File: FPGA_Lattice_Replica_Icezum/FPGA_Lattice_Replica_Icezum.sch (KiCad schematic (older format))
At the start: 0 parts

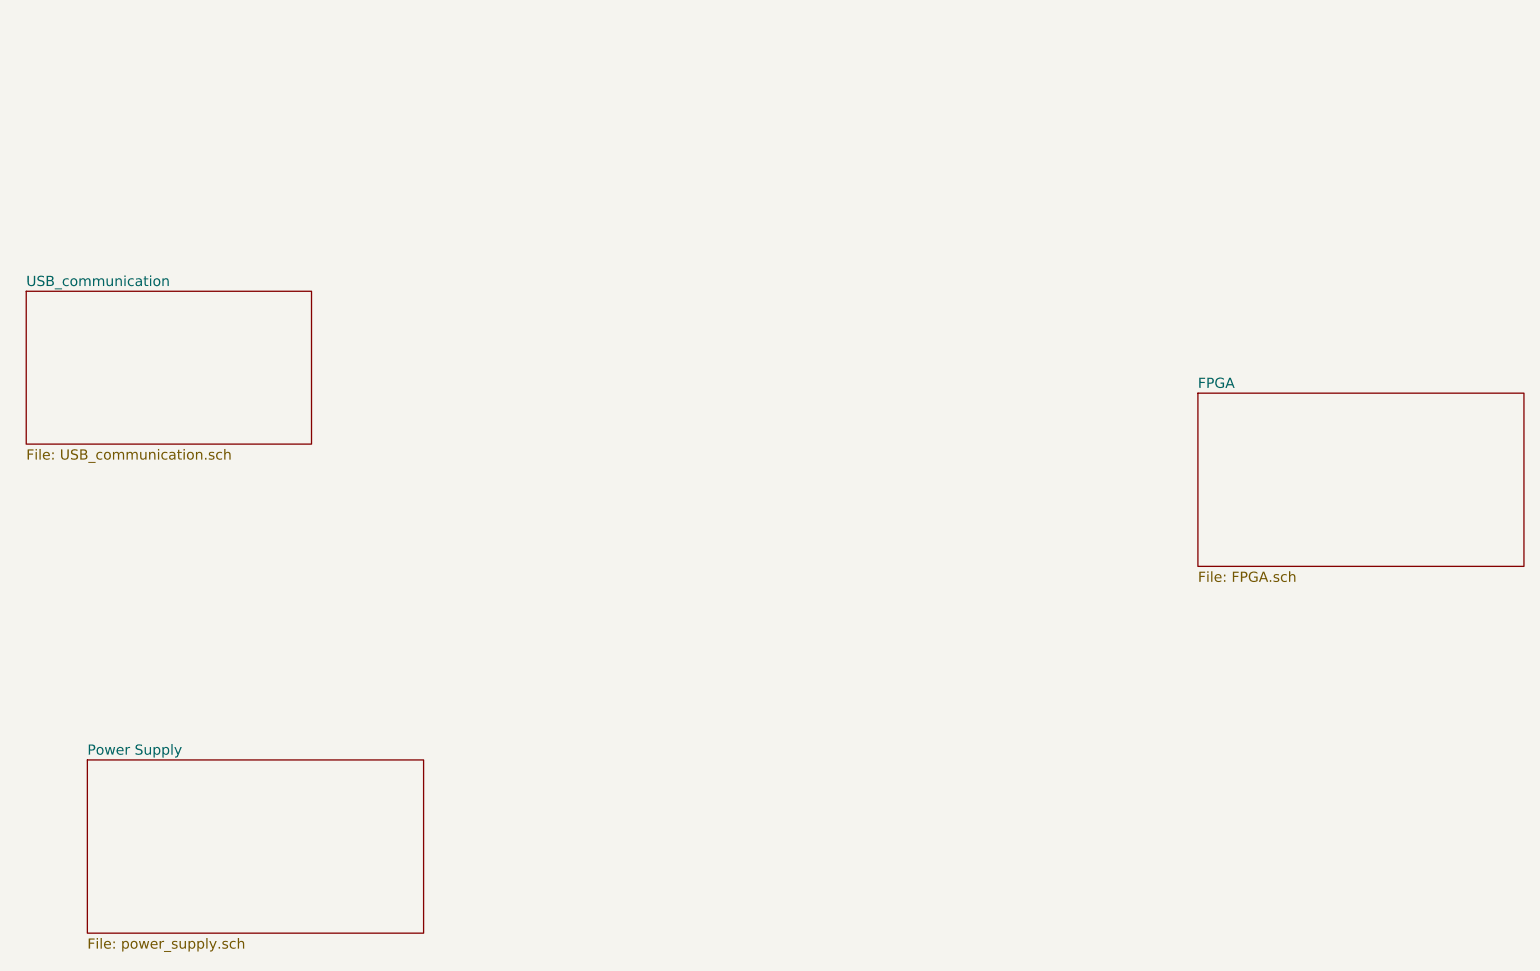
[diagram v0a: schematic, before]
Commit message: se completo esquema de perifericos y sockets. Se puso el mismo simbolo de referencia GND en el esquema de la fuente
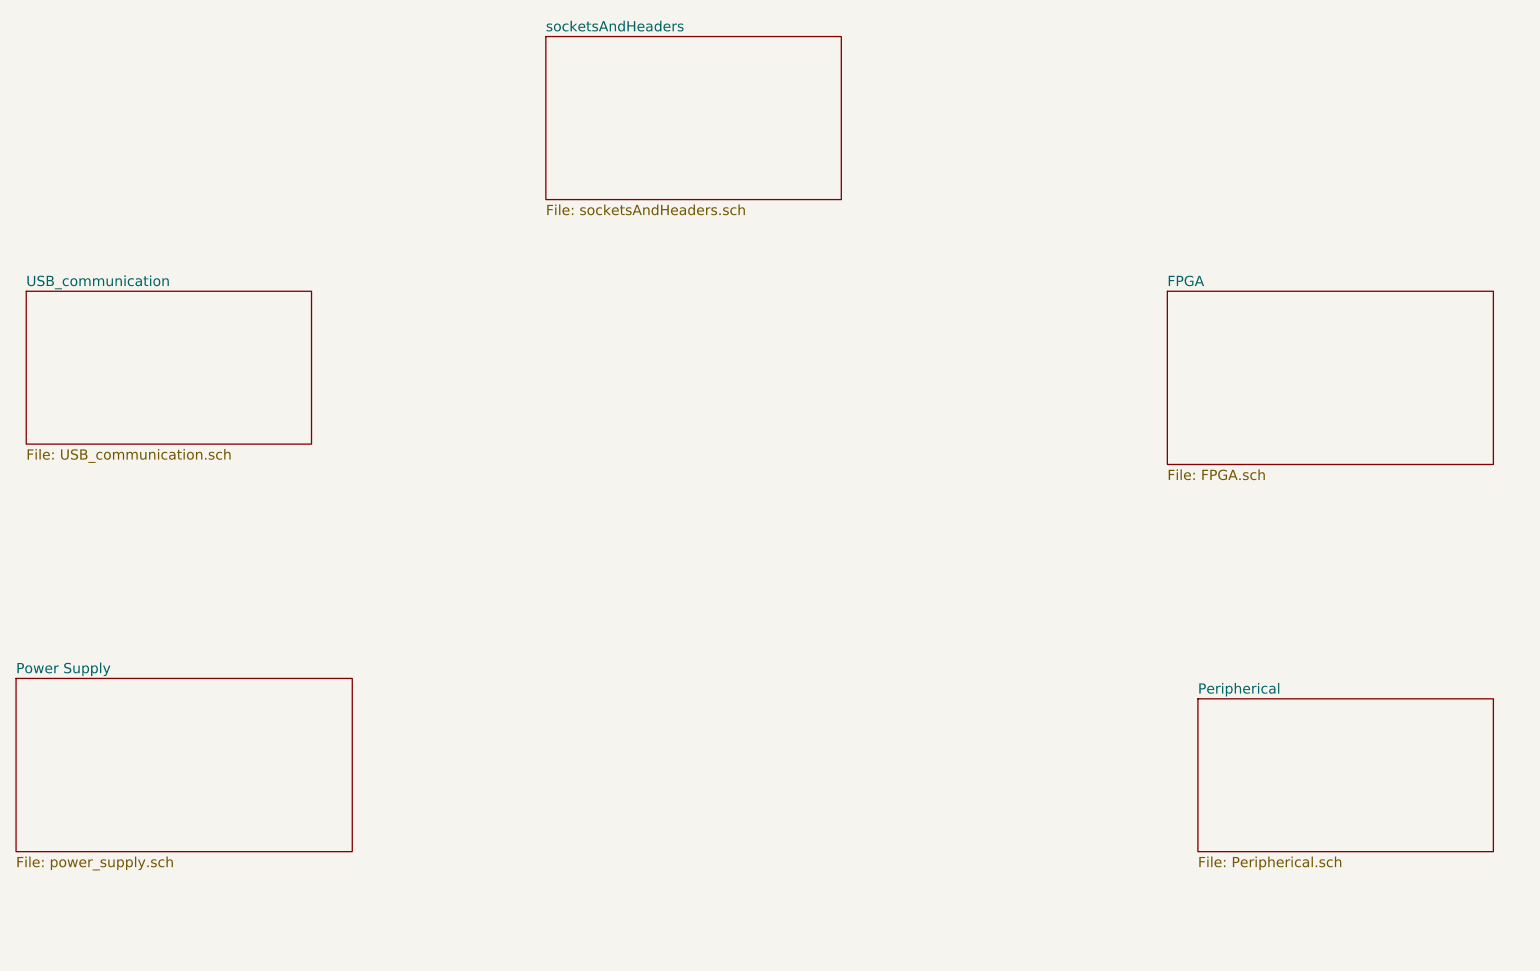
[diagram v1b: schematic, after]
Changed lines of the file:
@@
 $Descr A4 11693 8268
 encoding utf-8
-Sheet 1 4
+Sheet 1 6
 Title "Replica IceZUM FPGA board basado en FPGA Lattice ICE40HX1K"
 Date "2019-06-03"
@@
 $EndDescr
 $Sheet
-S 2700 4950 1650 850
+S 2350 4550 1650 850
 U 5CF4FEF6
 F0 "Power Supply" 50
@@
 $EndSheet
 $Sheet
-S 8150 3150 1600 850
+S 8000 2650 1600 850
 U 5CF846EC
 F0 "FPGA" 50
@@
 F1 "USB_communication.sch" 50
 $EndSheet
+$Sheet
+S 8150 4650 1450 750
+U 5D1D3861
+F0 "Peripherical" 50
+F1 "Peripherical.sch" 50
+$EndSheet
+$Sheet
+S 4950 1400 1450 800
+U 5CFE1C7D
+F0 "socketsAndHeaders" 50
+F1 "socketsAndHeaders.sch" 50
+$EndSheet
 $EndSCHEMATC

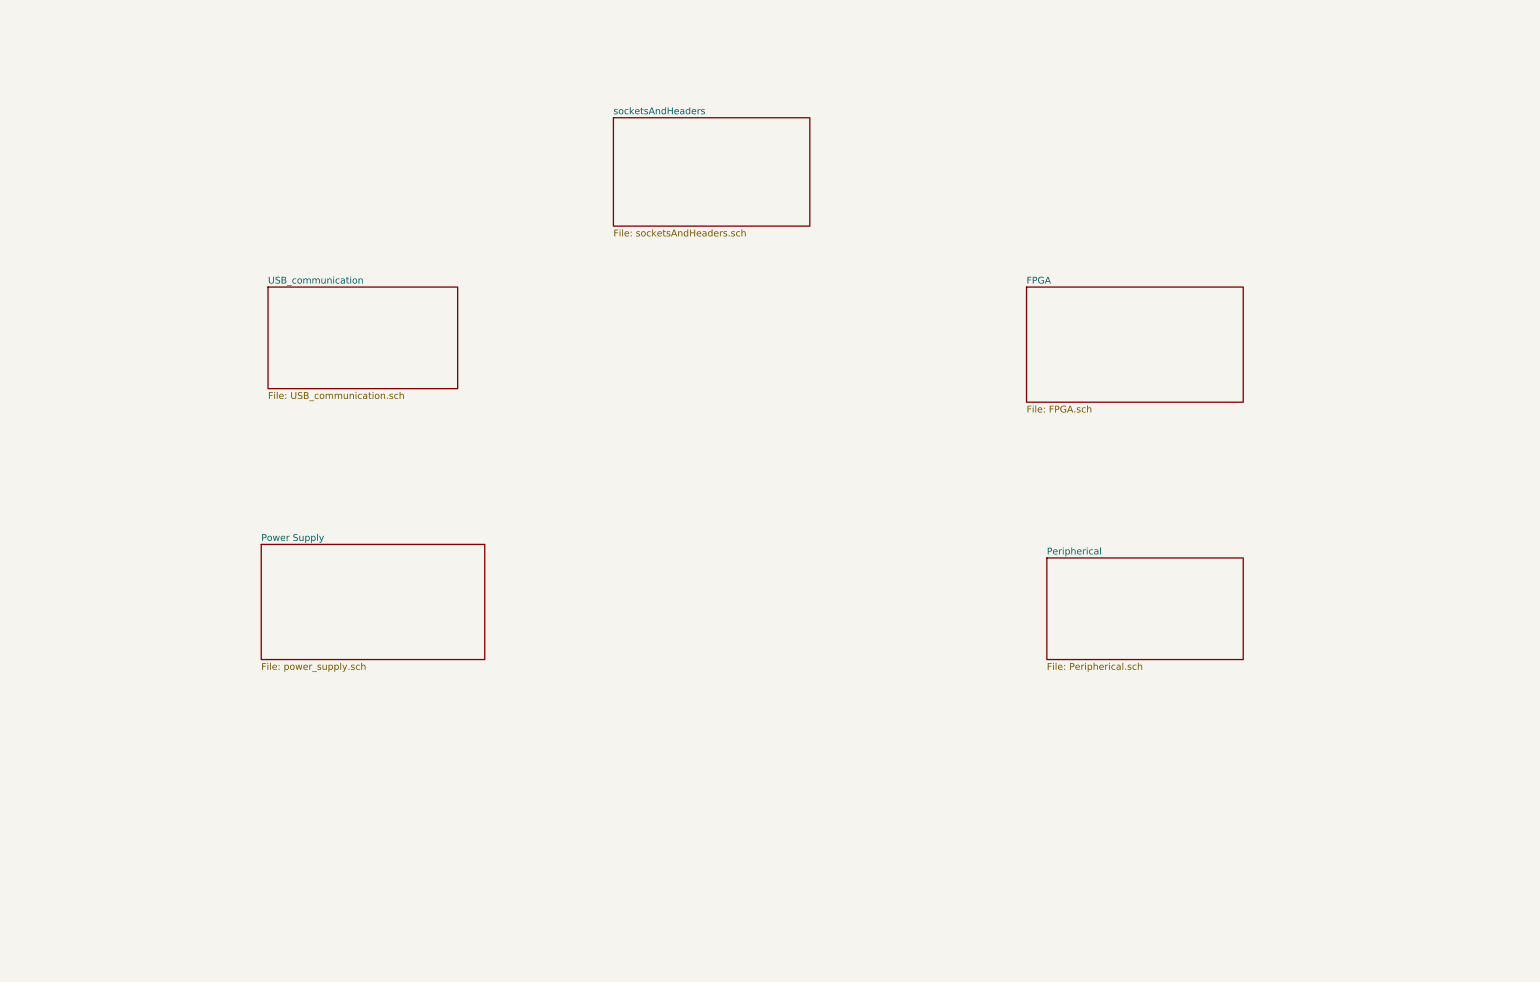
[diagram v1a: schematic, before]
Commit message: se comenzo asignacion de footprints
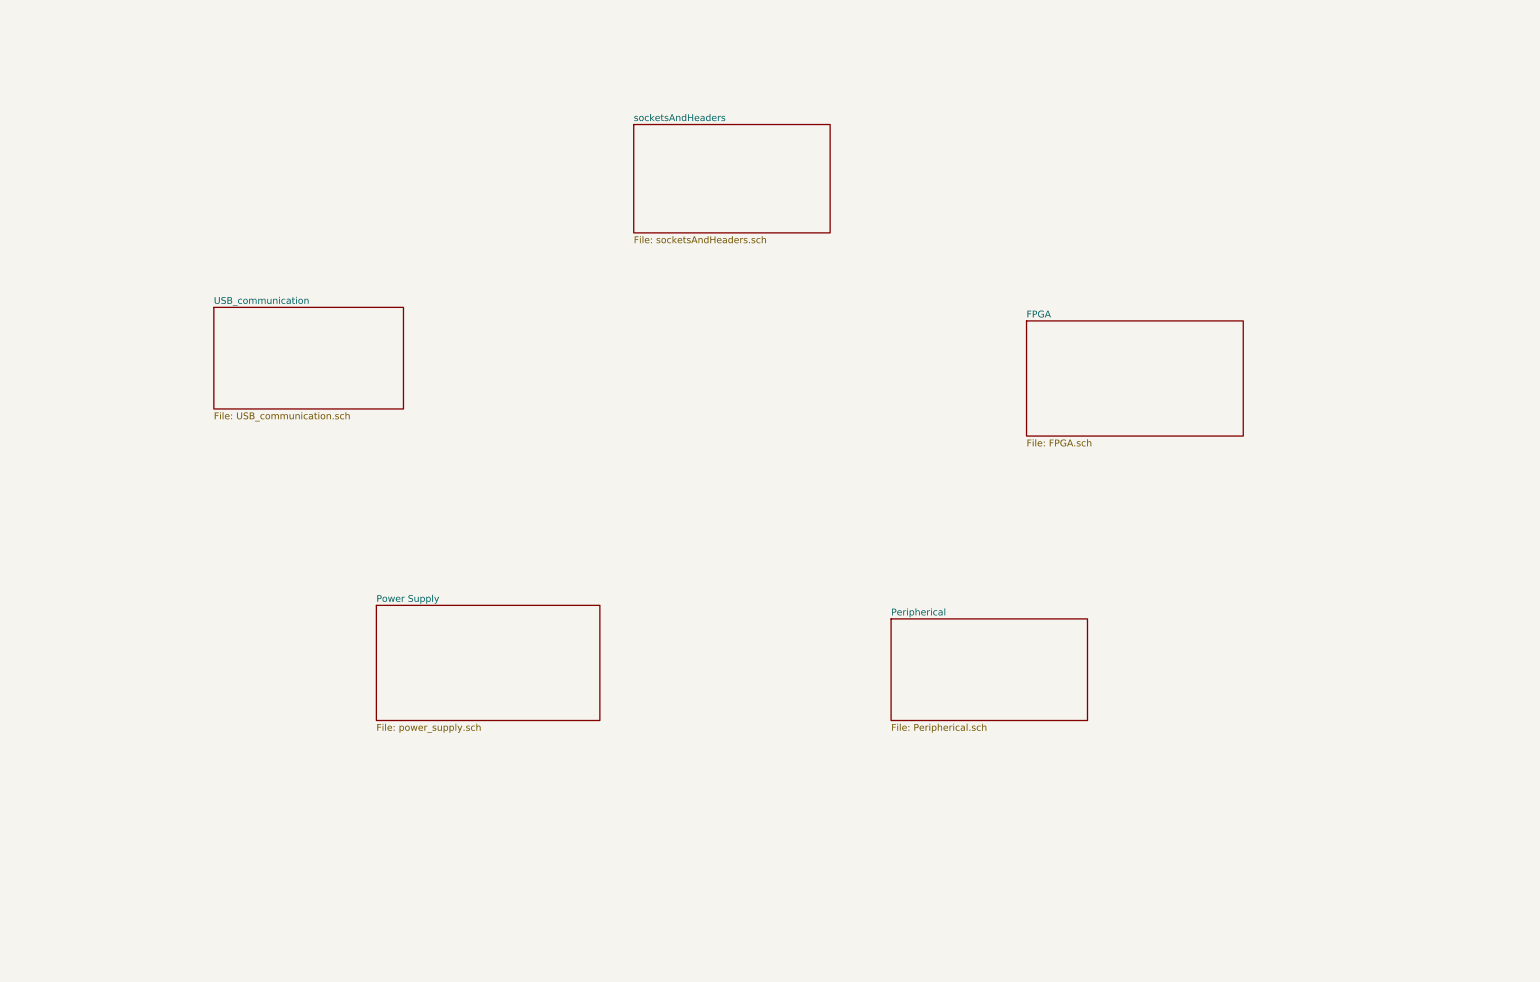
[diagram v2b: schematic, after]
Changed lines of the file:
@@
 $EndDescr
 $Sheet
-S 2350 4550 1650 850
+S 3200 5000 1650 850
 U 5CF4FEF6
 F0 "Power Supply" 50
@@
 $EndSheet
 $Sheet
-S 8000 2650 1600 850
+S 8000 2900 1600 850
 U 5CF846EC
 F0 "FPGA" 50
@@
 $EndSheet
 $Sheet
-S 2400 2650 1400 750
+S 2000 2800 1400 750
 U 5D2E3A88
 F0 "USB_communication" 50
@@
 $EndSheet
 $Sheet
-S 8150 4650 1450 750
+S 7000 5100 1450 750
 U 5D1D3861
 F0 "Peripherical" 50
@@
 $EndSheet
 $Sheet
-S 4950 1400 1450 800
+S 5100 1450 1450 800
 U 5CFE1C7D
 F0 "socketsAndHeaders" 50

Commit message: se finalizo asignación de footprint de acuerdo al modelo original de la icezum alhambra
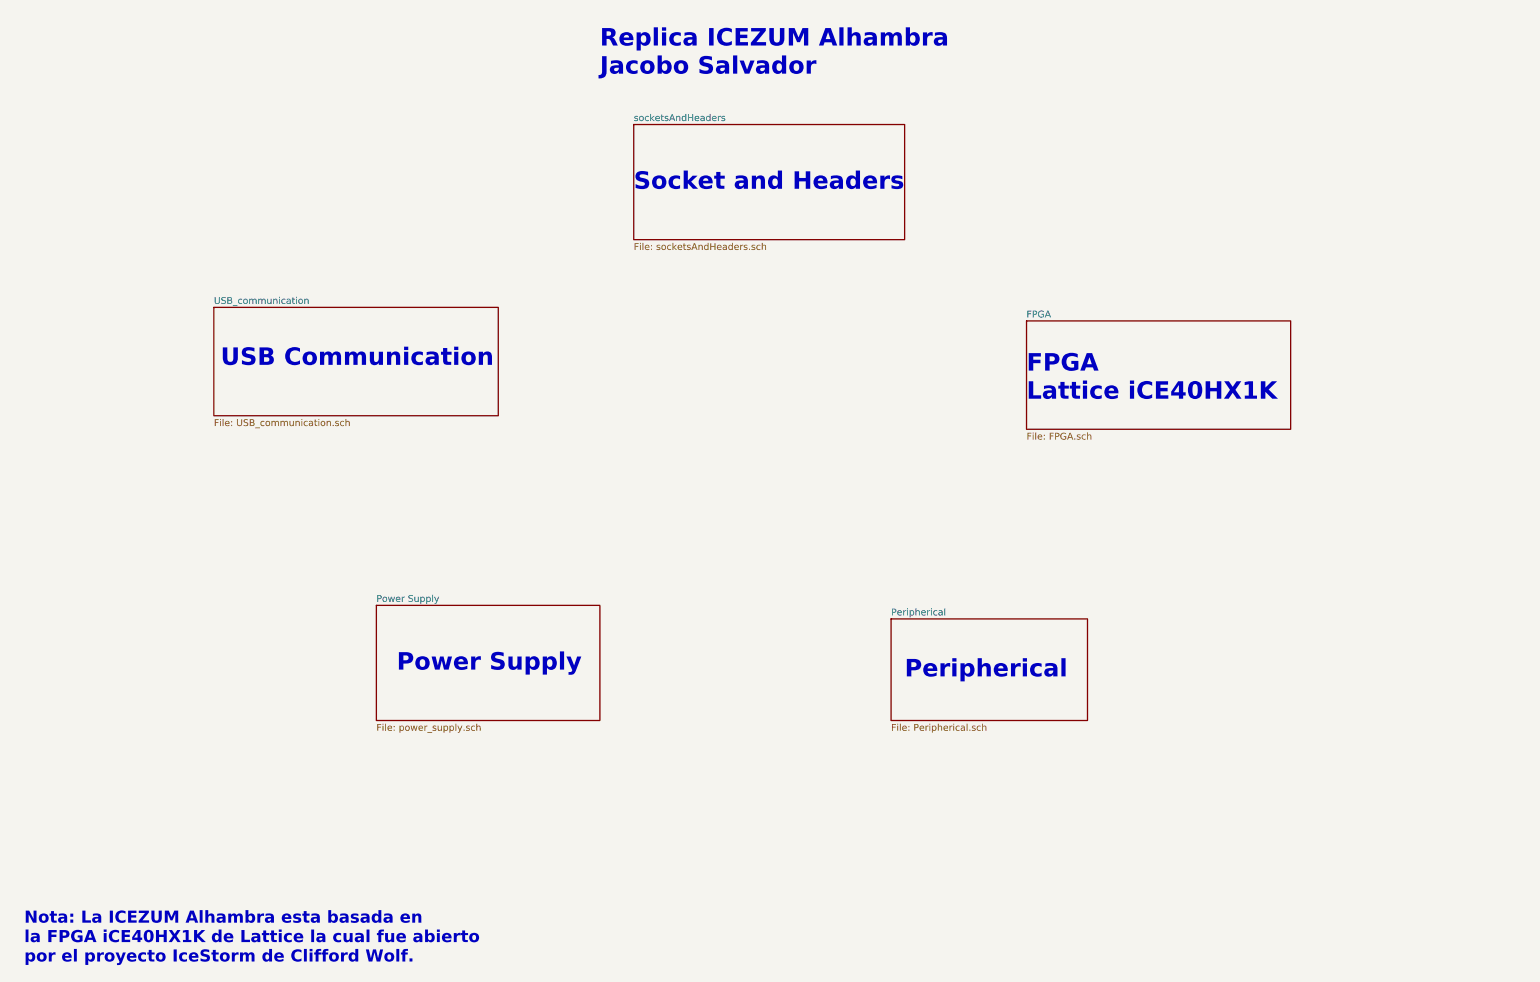
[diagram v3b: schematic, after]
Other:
- note added: "FPGA \nLattice iCE40HX1K"
- note added: "Nota: La ICEZUM Alhambra esta basada en\nla FPGA iCE40HX1K de Lattice la cual fue abierto \npor el proyecto IceStorm de Clifford Wolf."
- note added: "Peripherical\n"
- note added: "Power Supply"
- note added: "Replica ICEZUM Alhambra\nJacobo Salvador"
- note added: "Socket and Headers"
- note added: "USB Communication"
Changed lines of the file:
@@
 $EndSheet
 $Sheet
-S 8000 2900 1600 850
+S 8000 2900 1950 800
 U 5CF846EC
 F0 "FPGA" 50
@@
 $EndSheet
 $Sheet
-S 2000 2800 1400 750
+S 2000 2800 2100 800
 U 5D2E3A88
 F0 "USB_communication" 50
@@
 $EndSheet
 $Sheet
-S 5100 1450 1450 800
+S 5100 1450 2000 850
 U 5CFE1C7D
 F0 "socketsAndHeaders" 50
 F1 "socketsAndHeaders.sch" 50
 $EndSheet
+Text Notes 3350 5500 0    129  ~ 26
+Power Supply
+Text Notes 7100 5550 0    129  ~ 26
+Peripherical\n
+Text Notes 2050 3250 0    129  ~ 26
+USB Communication
+Text Notes 8000 3500 0    129  ~ 26
+FPGA \nLattice iCE40HX1K
+Text Notes 5100 1950 0    129  ~ 26
+Socket and Headers
+Text Notes 4850 1100 0    129  ~ 26
+Replica ICEZUM Alhambra\nJacobo Salvador
+Text Notes 600  7650 0    89   ~ 18
+Nota: La ICEZUM Alhambra esta basada en\nla FPGA iCE40HX1K de Lattice la cual fue abierto \npor el proyecto IceStorm de Clifford Wolf.
 $EndSCHEMATC

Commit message: se coloco hojas de datos de los componentes
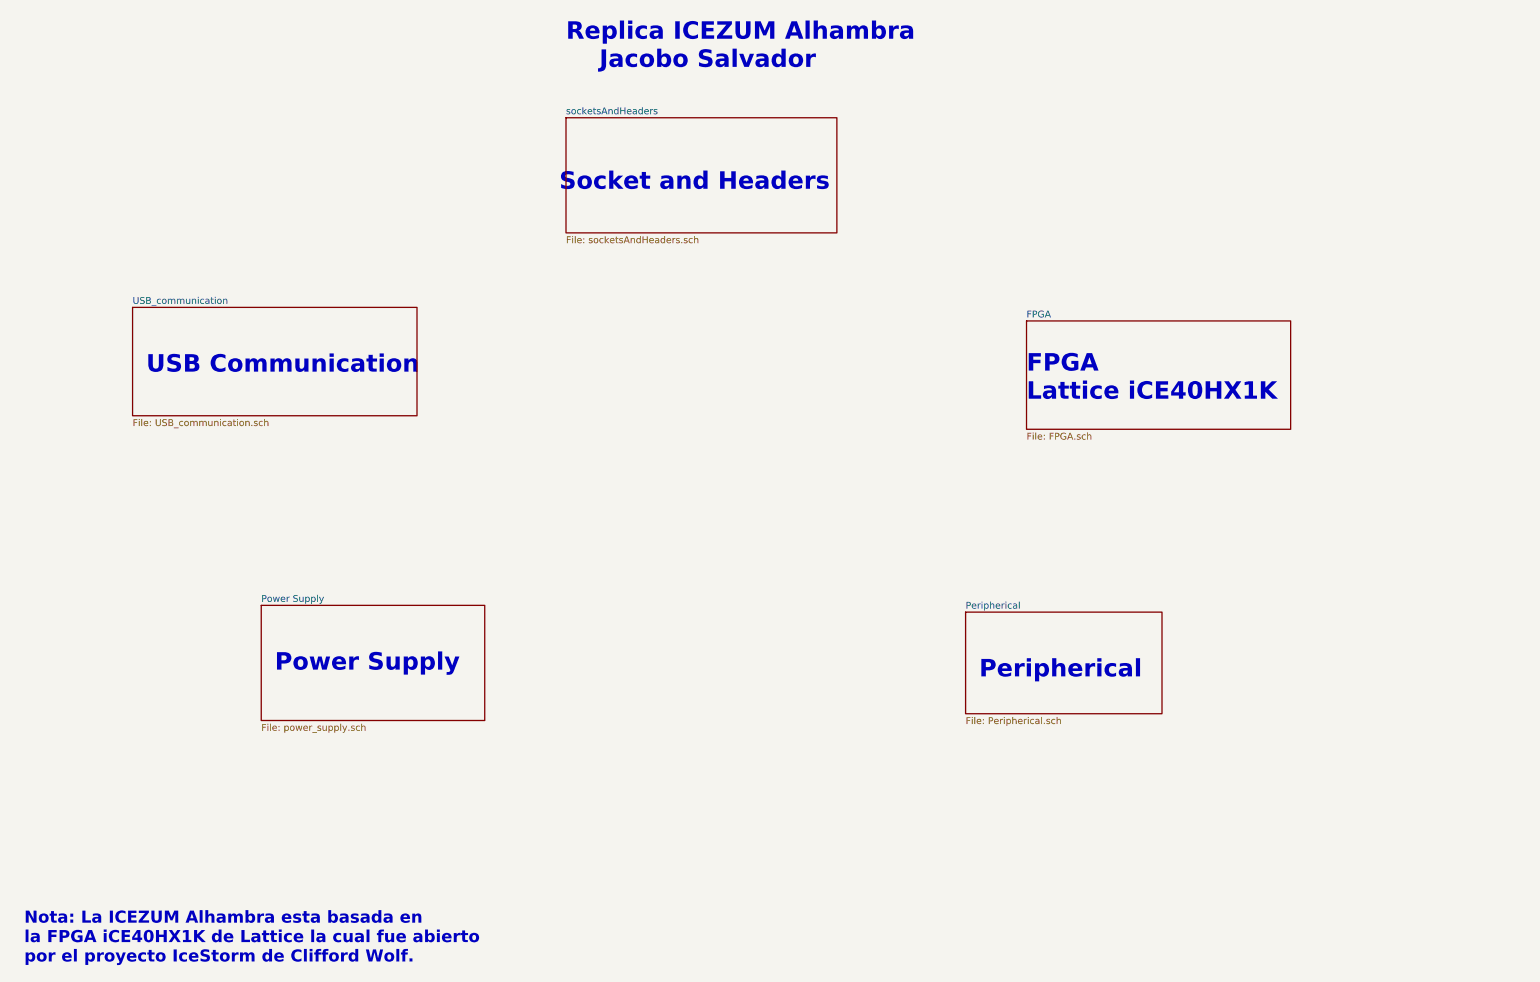
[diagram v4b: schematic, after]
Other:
- note added: "Replica ICEZUM Alhambra\n Jacobo Salvador"
- note removed: "Replica ICEZUM Alhambra\nJacobo Salvador"
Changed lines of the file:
@@
 $EndDescr
 $Sheet
-S 3200 5000 1650 850
+S 2350 5000 1650 850
 U 5CF4FEF6
 F0 "Power Supply" 50
@@
 $EndSheet
 $Sheet
-S 2000 2800 2100 800
+S 1400 2800 2100 800
 U 5D2E3A88
 F0 "USB_communication" 50
@@
 $EndSheet
 $Sheet
-S 7000 5100 1450 750
+S 7550 5050 1450 750
 U 5D1D3861
 F0 "Peripherical" 50
@@
 $EndSheet
 $Sheet
-S 5100 1450 2000 850
+S 4600 1400 2000 850
 U 5CFE1C7D
 F0 "socketsAndHeaders" 50
 F1 "socketsAndHeaders.sch" 50
 $EndSheet
-Text Notes 3350 5500 0    129  ~ 26
+Text Notes 2450 5500 0    129  ~ 26
 Power Supply
-Text Notes 7100 5550 0    129  ~ 26
+Text Notes 7650 5550 0    129  ~ 26
 Peripherical\n
-Text Notes 2050 3250 0    129  ~ 26
+Text Notes 1500 3300 0    129  ~ 26
 USB Communication
 Text Notes 8000 3500 0    129  ~ 26
 FPGA \nLattice iCE40HX1K
-Text Notes 5100 1950 0    129  ~ 26
+Text Notes 4550 1950 0    129  ~ 26
 Socket and Headers
-Text Notes 4850 1100 0    129  ~ 26
-Replica ICEZUM Alhambra\nJacobo Salvador
+Text Notes 4600 1050 0    129  ~ 26
+Replica ICEZUM Alhambra\n    Jacobo Salvador
 Text Notes 600  7650 0    89   ~ 18
 Nota: La ICEZUM Alhambra esta basada en\nla FPGA iCE40HX1K de Lattice la cual fue abierto \npor el proyecto IceStorm de Clifford Wolf.
